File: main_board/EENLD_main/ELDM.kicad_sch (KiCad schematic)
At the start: 24 parts, among them J301 Conn_01x02_Socket, Q301 AO3400A, U301 AD5160BRJZ5, U302 RT9187QV

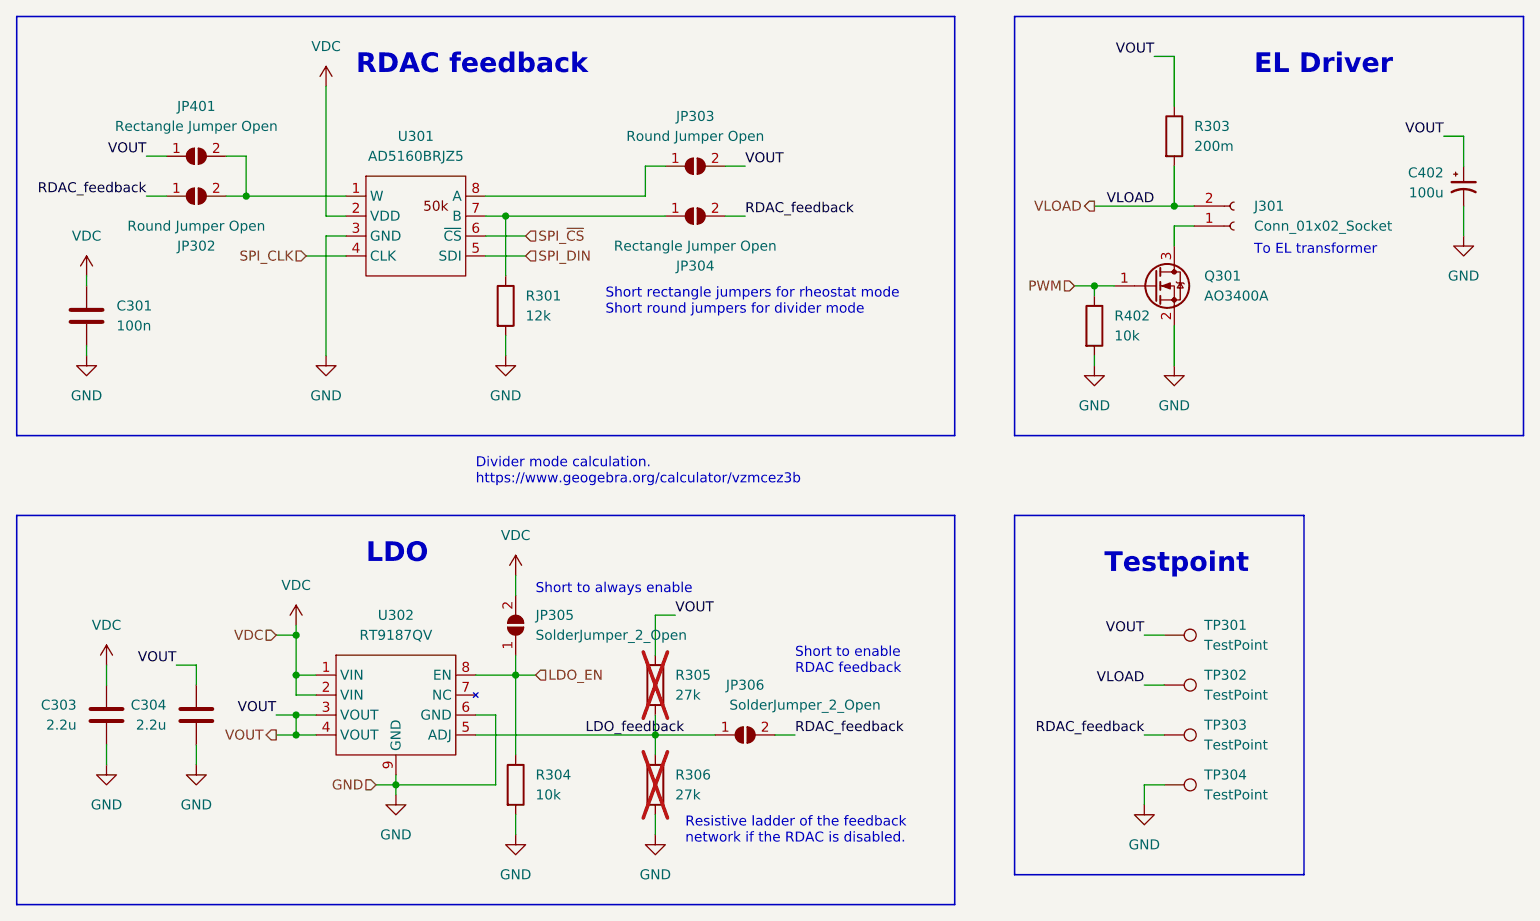
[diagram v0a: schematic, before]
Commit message: Finished PCB layout v0.1.
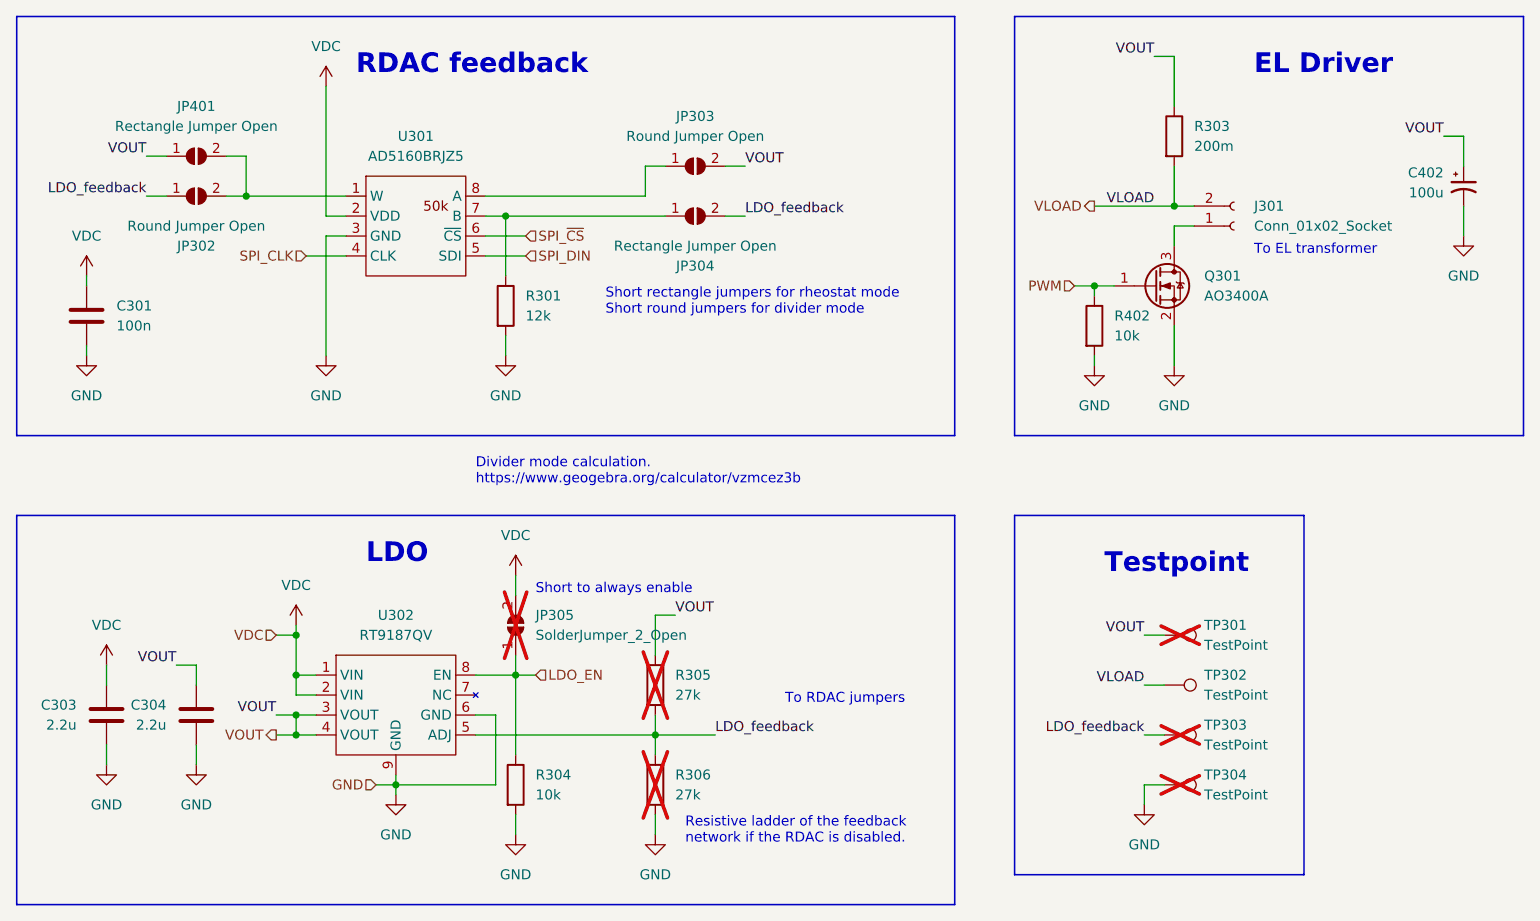
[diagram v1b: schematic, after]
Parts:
- removed JP306: SolderJumper_2_Open, symbol Jumper:SolderJumper_2_Open
- C301: footprint (none) -> Capacitor_SMD:C_0603_1608Metric_Pad1.08x0.95mm_HandSolder; LCSC (none) -> C14663
- C303, C304: footprint (none) -> Capacitor_SMD:C_0805_2012Metric_Pad1.18x1.45mm_HandSolder; LCSC (none) -> C377773
- C402: footprint (none) -> Capacitor_THT:CP_Radial_D8.0mm_P2.50mm
- J301: footprint (none) -> Connector_Wire:SolderWire-1.5sqmm_1x02_P7.8mm_D1.7mm_OD3.9mm
- JP302, JP303: footprint (none) -> Jumper:SolderJumper-2_P1.3mm_Open_RoundedPad1.0x1.5mm
- JP305: footprint (none) -> Jumper:SolderJumper-2_P1.3mm_Open_Pad1.0x1.5mm; now not fitted; now left out of the parts list
- Q301: LCSC (none) -> C20917
- R301: footprint (none) -> Resistor_SMD:R_0402_1005Metric_Pad0.72x0.64mm_HandSolder; LCSC (none) -> C25752
- R303: footprint (none) -> Resistor_SMD:R_2512_6332Metric_Pad1.40x3.35mm_HandSolder; LCSC (none) -> C309648
- R304, R402: footprint (none) -> Resistor_SMD:R_0402_1005Metric_Pad0.72x0.64mm_HandSolder; LCSC (none) -> C25744
- TP301, TP303, TP304: footprint (none) -> TestPoint:TestPoint_THTPad_D1.5mm_Drill0.7mm; now not fitted; now left out of the parts list
- TP302: footprint (none) -> TestPoint:TestPoint_THTPad_D1.5mm_Drill0.7mm; now left out of the parts list
- U301: LCSC (none) -> C578142
- U302: LCSC (none) -> C147970
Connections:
- net RDAC_feedback is gone; now on net LDO_feedback: JP302.1 (A), JP304.2 (B), TP303.1
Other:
- note added: "To RDAC jumpers"
- note removed: "Short to enable RDAC feedback"

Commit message: added midi2array
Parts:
- C402, J301, JP302, JP303, JP304, JP401: now left out of the parts list
- Q301: JLCPCB Rotation Offset (none) -> 180
- U301, U302: JLCPCB Rotation Offset (none) -> -90
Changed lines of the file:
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@@
       (effects (font (size 1.27 1.27)) hide)
     )
-    (property "JLCPCB Rotation Offset" "" (at 71.12 40.64 0)
+    (property "JLCPCB Rotation Offset" "-90" (at 71.12 40.64 0)
       (effects (font (size 1.27 1.27)) hide)
     )
@@
   )
   (symbol (lib_id "Connector:Conn_01x02_Socket") (at 175.26 46.99 0) (mirror x) (unit 1)
-    (in_bom yes) (on_board yes) (dnp no)
+    (in_bom no) (on_board yes) (dnp no)
     (property "Reference" "J301" (at 177.8 44.45 0)
       (effects (font (size 1.27 1.27)) (justify left))
@@
   )
   (symbol (lib_id "Jumper:SolderJumper_2_Open") (at 43.18 38.1 0) (unit 1)
-    (in_bom yes) (on_board yes) (dnp no) (fields_autoplaced)
+    (in_bom no) (on_board yes) (dnp no) (fields_autoplaced)
     (property "Reference" "JP401" (at 43.18 31.75 0)
       (effects (font (size 1.27 1.27)))
@@
       (effects (font (size 1.27 1.27)) (justify left) hide)
     )
-    (property "JLCPCB Rotation Offset" "" (at 165.1 54.61 0)
+    (property "JLCPCB Rotation Offset" "180" (at 165.1 54.61 0)
       (effects (font (size 1.27 1.27)) hide)
     )
@@
   )
   (symbol (lib_id "Device:C_Polarized_Small_US") (at 204.47 41.91 0) (unit 1)
-    (in_bom yes) (on_board yes) (dnp no)
+    (in_bom no) (on_board yes) (dnp no)
     (property "Reference" "C402" (at 201.93 40.2082 0)
       (effects (font (size 1.27 1.27)) (justify right))
@@
   )
   (symbol (lib_id "Jumper:SolderJumper_2_Open") (at 43.18 43.18 0) (mirror x) (unit 1)
-    (in_bom yes) (on_board yes) (dnp no)
+    (in_bom no) (on_board yes) (dnp no)
     (property "Reference" "JP302" (at 43.18 49.53 0)
       (effects (font (size 1.27 1.27)))
@@
       (effects (font (size 1.27 1.27)) hide)
     )
-    (property "JLCPCB Rotation Offset" "" (at 68.58 101.6 0)
+    (property "JLCPCB Rotation Offset" "-90" (at 68.58 101.6 0)
       (effects (font (size 1.27 1.27)) hide)
     )
@@
   )
   (symbol (lib_id "Jumper:SolderJumper_2_Open") (at 106.68 45.72 0) (mirror x) (unit 1)
-    (in_bom yes) (on_board yes) (dnp no)
+    (in_bom no) (on_board yes) (dnp no)
     (property "Reference" "JP304" (at 106.68 52.07 0)
       (effects (font (size 1.27 1.27)))
@@
   )
   (symbol (lib_id "Jumper:SolderJumper_2_Open") (at 106.68 39.37 0) (unit 1)
-    (in_bom yes) (on_board yes) (dnp no)
+    (in_bom no) (on_board yes) (dnp no)
     (property "Reference" "JP303" (at 106.68 33.02 0)
       (effects (font (size 1.27 1.27)))
